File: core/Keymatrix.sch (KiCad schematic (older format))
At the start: 180 parts

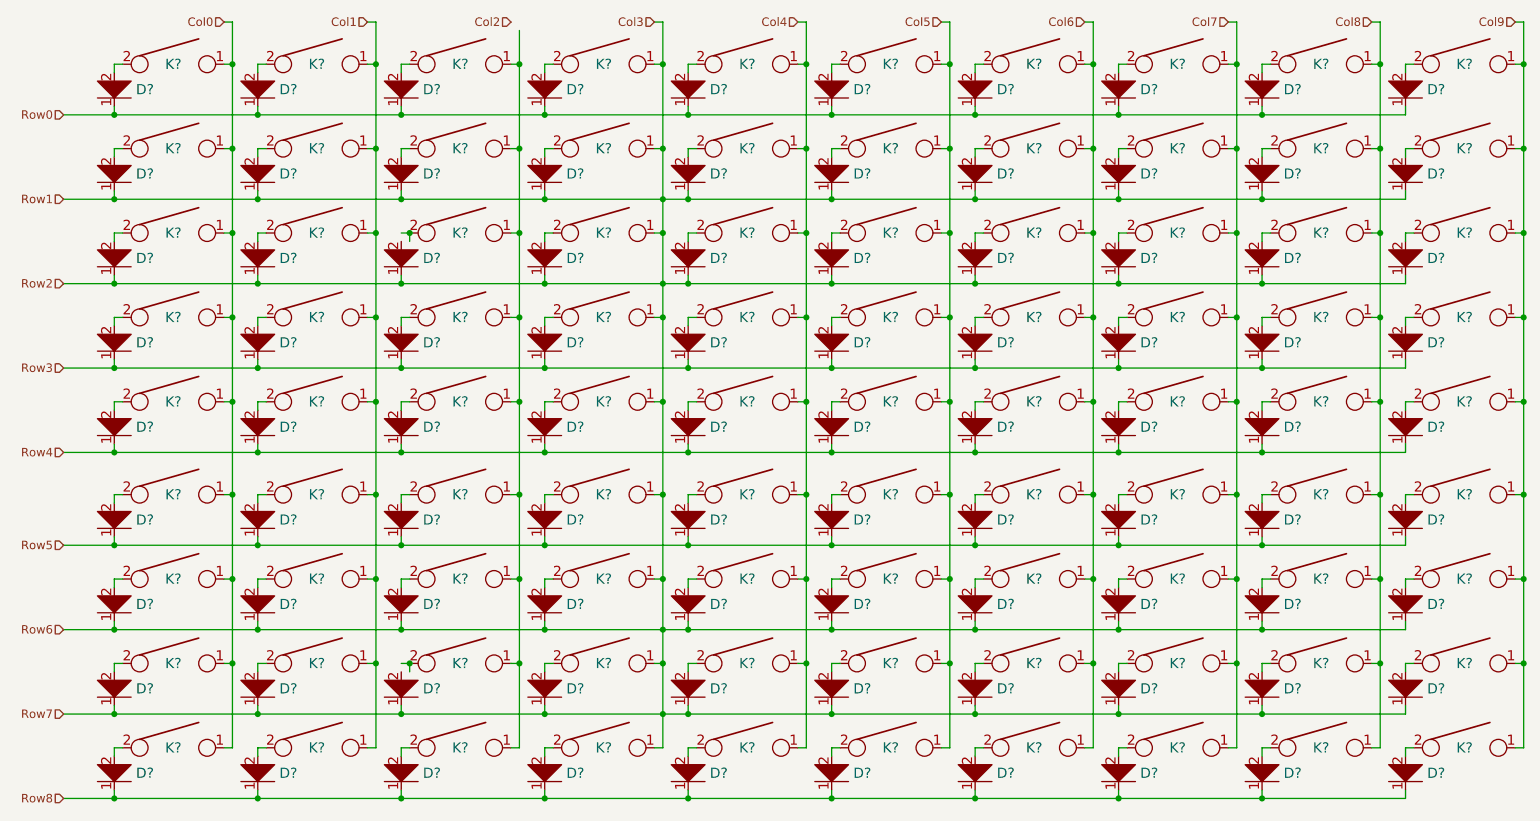
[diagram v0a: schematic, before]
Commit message: move LEDs into their own sheets
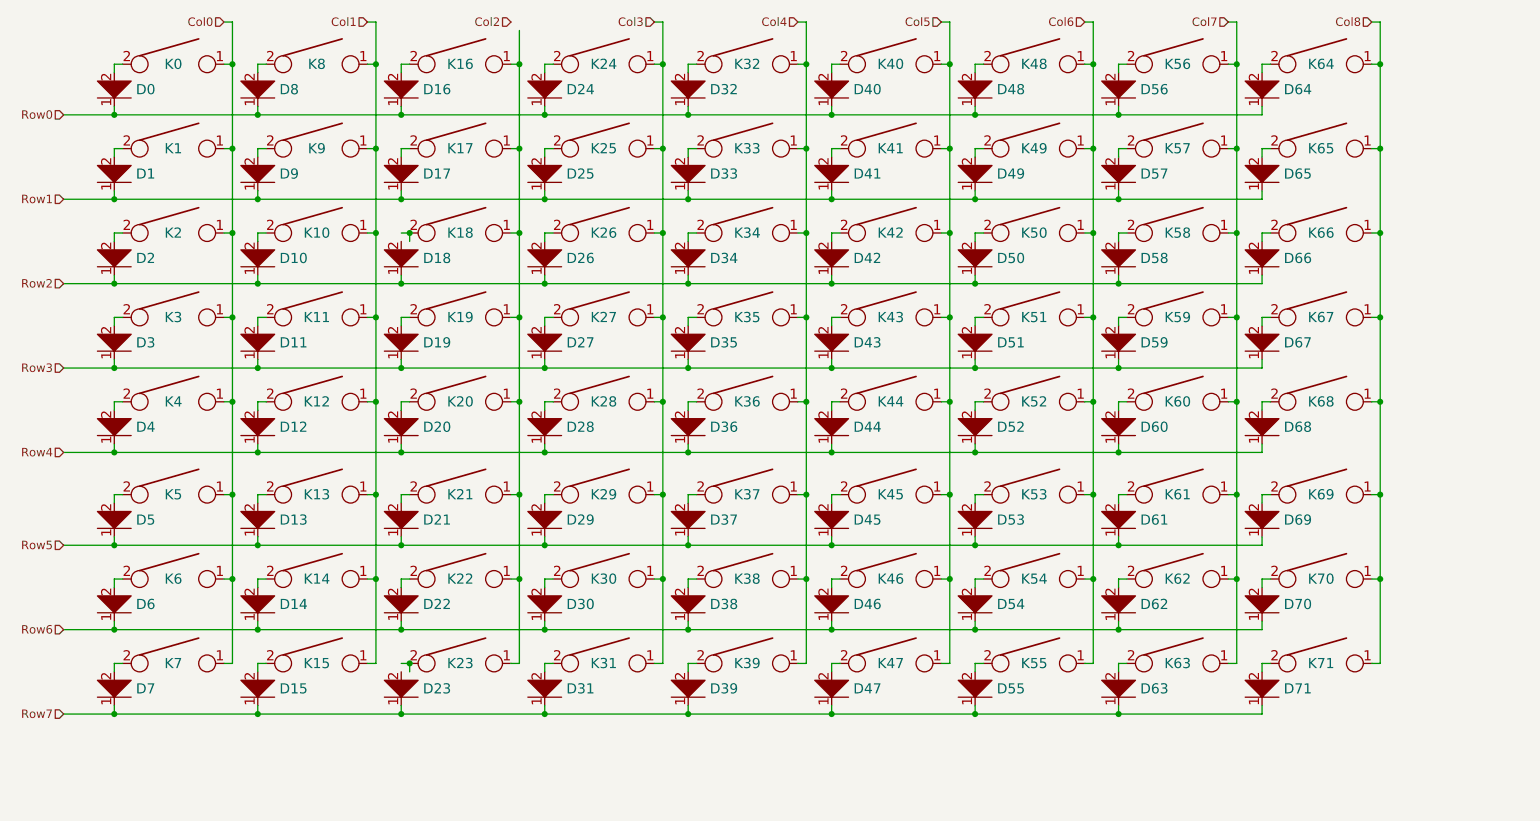
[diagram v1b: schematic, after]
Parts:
- removed D? (x18): D, keyboard_parts:D_SOD123_axial, symbol core-rescue:D-keyboard_parts
- removed K? (x18): KEYSW, keyswitches:Kailh_socket, symbol core-rescue:KEYSW-keyboard_parts
- gave numbers to parts that had none: 144
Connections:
- net Col3: no longer D1.1, D10.1, D14.1, D15.1, D17.1, D18.1, D2.1, D22.1, D23.1, D25.1, D26.1, D30.1, D31.1, D33.1, D34.1, D38.1, D39.1, D41.1, D42.1, D46.1, D47.1, D49.1, D50.1, D54.1, D55.1, D57.1, D58.1, D6.1, D62.1, D63.1, D65.1, D66.1, D7.1, D70.1, D71.1, D9.1
- new net Row1: D1.1, D17.1, D25.1, D33.1, D41.1, D49.1, D57.1, D65.1, D9.1
- new net Row2: D10.1, D18.1, D2.1, D26.1, D34.1, D42.1, D50.1, D58.1, D66.1
- new net Row6: D14.1, D22.1, D30.1, D38.1, D46.1, D54.1, D6.1, D62.1, D70.1
- new net Row7: D15.1, D23.1, D31.1, D39.1, D47.1, D55.1, D63.1, D7.1, D71.1
